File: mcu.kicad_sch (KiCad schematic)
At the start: 39 parts, among them J10 ${MANUFACTURER PART NUMBER}, J11 ${MANUFACTURER PART NUMBER}, J8 ${MANUFACTURER PART NUMBER}, J9 ${MANUFACTURER PART NUMBER}, U1 ${MANUFACTURER PART NUMBER}, U5 ${MANUFACTURER PART NUMBER}, U6 USBLC6-2P6, Y1 ${FREQUENCY}

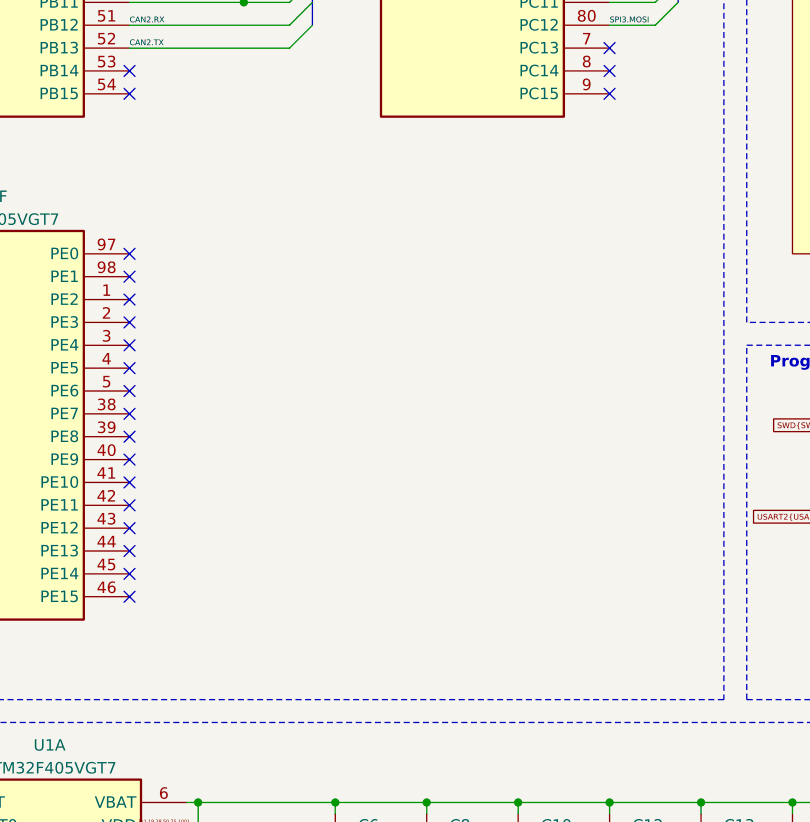
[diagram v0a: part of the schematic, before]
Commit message: - On push in main create a new set of documents - On release fix images - Update README to use correct images
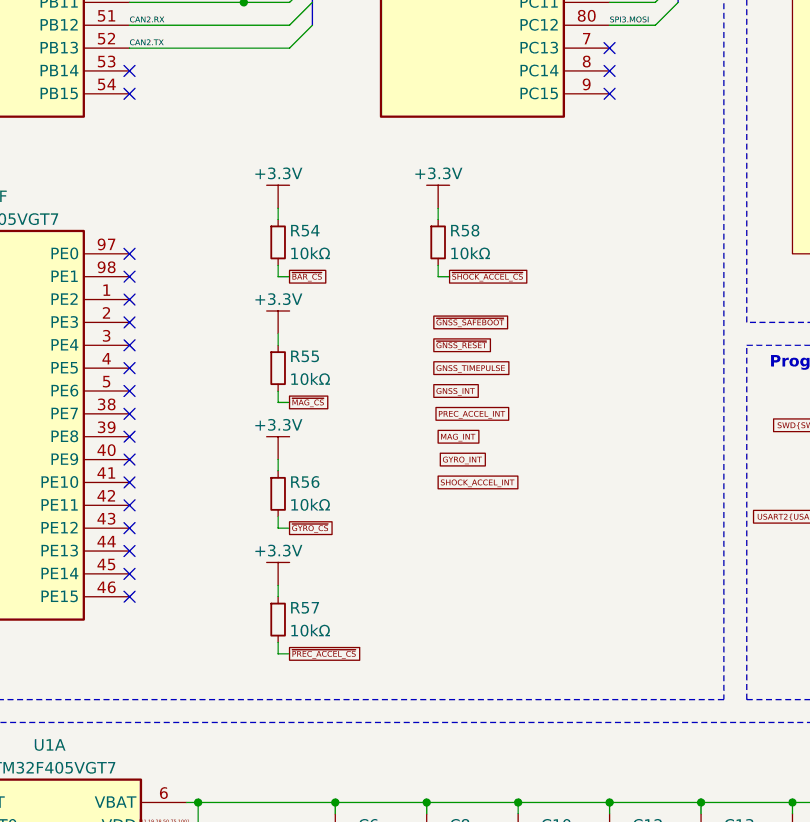
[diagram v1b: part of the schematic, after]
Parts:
- added R54, R55, R56, R57, R58: ${RESISTANCE}, passive_resistor:R_0603_Density_Nominal, symbol passive_resistor:CRCW060310K0FKEAHP
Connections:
- net +3.3V: now also R54.1, R55.1, R56.1, R57.1, R58.1
- new net ~{BAR_CS}: R54.2
- new net ~{GYRO_CS}: R56.2
- new net ~{MAG_CS}: R55.2
- new net ~{PREC_ACCEL_CS}: R57.2
- new net ~{SHOCK_ACCEL_CS}: R58.2

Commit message: Major fix: move from a flat to a hierarchical architecture for schematic.
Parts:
- removed C1, C10, C12, C13, C16, C21, C26, C6, C8, C9: ${CAPACITANCE}, passive_capacitor:C_0603_Density_Nominal, symbol passive_capacitor:C0603C104J3RACAUTO
- removed C11: ${CAPACITANCE}, passive_capacitor:C_0805_Density_Nominal, symbol passive_capacitor:C0805C105J3RECAUTO
- removed C2, C3: ${CAPACITANCE}, passive_capacitor:C_0603_Density_Nominal, symbol passive_capacitor:CGA3E2C0G1H060D080AA
- removed C22: ${CAPACITANCE}, passive_capacitor:C_1206_Density_Nominal, symbol passive_capacitor:C1206F475K4RACAUTO
- removed C5, C7: ${CAPACITANCE}, passive_capacitor:C_0805_Density_Nominal, symbol passive_capacitor:C0805C225K4RECAUTO
- removed D10, D11, D12, D13, D14, D8, D9: (no value), passive_diode:SZESD7351HT1G, symbol passive_diode:SZESD7351HT1G
- removed J10: ${MANUFACTURER PART NUMBER}, electromechanical_connector:TSW-102-07-F-S, symbol electromechanical_connector:TSW-102-07-F-S
- removed J11: ${MANUFACTURER PART NUMBER}, electromechanical_connector:TSW-103-07-F-S, symbol electromechanical_connector:TSW-103-07-F-S
- removed J8: ${MANUFACTURER PART NUMBER}, electromechanical_connector:0530480810, symbol electromechanical_connector:0530480810
- removed J9: ${MANUFACTURER PART NUMBER}, electromechanical_connector:USB4105-GF-A-120, symbol electromechanical_connector:USB4105-GF-A-120
- removed R1, R34, R54, R55, R56, R57, R58: ${RESISTANCE}, passive_resistor:R_0603_Density_Nominal, symbol passive_resistor:CRCW060310K0FKEAHP
- removed R25, R26: ${RESISTANCE}, passive_resistor:R_0603_Density_Nominal, symbol passive_resistor:CRCW06031K80FKEAHP
- removed R46, R47: ${RESISTANCE}, passive_resistor:R_0603_Density_Nominal, symbol passive_resistor:CRCW06035K10FKEAHP
- removed R48: ${RESISTANCE}, passive_resistor:R_0603_Density_Nominal, symbol passive_resistor:CRCW060333K0FKEAHP
- removed R49: ${RESISTANCE}, passive_resistor:R_0603_Density_Nominal, symbol passive_resistor:CRCW060382K0FKEA
- removed U1: ${MANUFACTURER PART NUMBER}, ic_mcu:STM32F405VGT7, symbol ic_mcu:STM32F405VGT7
- removed U5: ${MANUFACTURER PART NUMBER}, ic_memory:S25FL256LAGNFM010, symbol ic_memory:S25FL256LAGNFM010
- removed U6: USBLC6-2P6, ic_protection:USBLC6-2P6, symbol ic_protection:USBLC6-2P6
- removed Y1: ${FREQUENCY}, passive_oscillator:ECS-250-8-33Q-RES-TR, symbol passive_oscillator:ECS-250-8-33Q-RES-TR
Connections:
- no-connect marks 55 -> 0
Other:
- note removed: "Buzzer PS1240P02BT"
- note removed: "F = 25MHz ESR = 40Ω C_{L} = 8pF C_{0} = 7pF C_{S} = 5pF g_{m} = 5 mA/V C_{tot} = C_{L} + (C_{S} / 2) C_{L1/2} = 2 × (C_{L} - C_{S}) = 6pF DL = (ESR × (π × F × C_{tot})^{2} × (V_{pp})^{2}) / 2 = 97.07μW g_{m critical} = 4 × (ESR) × (2 × π × F)^{2} × (C_{0} + C_{L})^{2} = 0.89 mA/V g_{m margin} = g_{m margin} / g_{m critical} = 5.63"
- note removed: "Memory"
- note removed: "Microcontroller bank A, B, C, D, E"
- note removed: "Microcontroller core"
- note removed: "Programming/debug connector"
- note removed: "USB connector"
